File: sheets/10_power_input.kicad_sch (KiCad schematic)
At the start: 36 parts, among them J1 MSTB 2,5/5-GF-5,08, J2 MSTB 2,5/2-GF-5,08, Q101 STD18NF25, Q102 IPD30N10S3L-34, U101 LM74930QRGERQ1

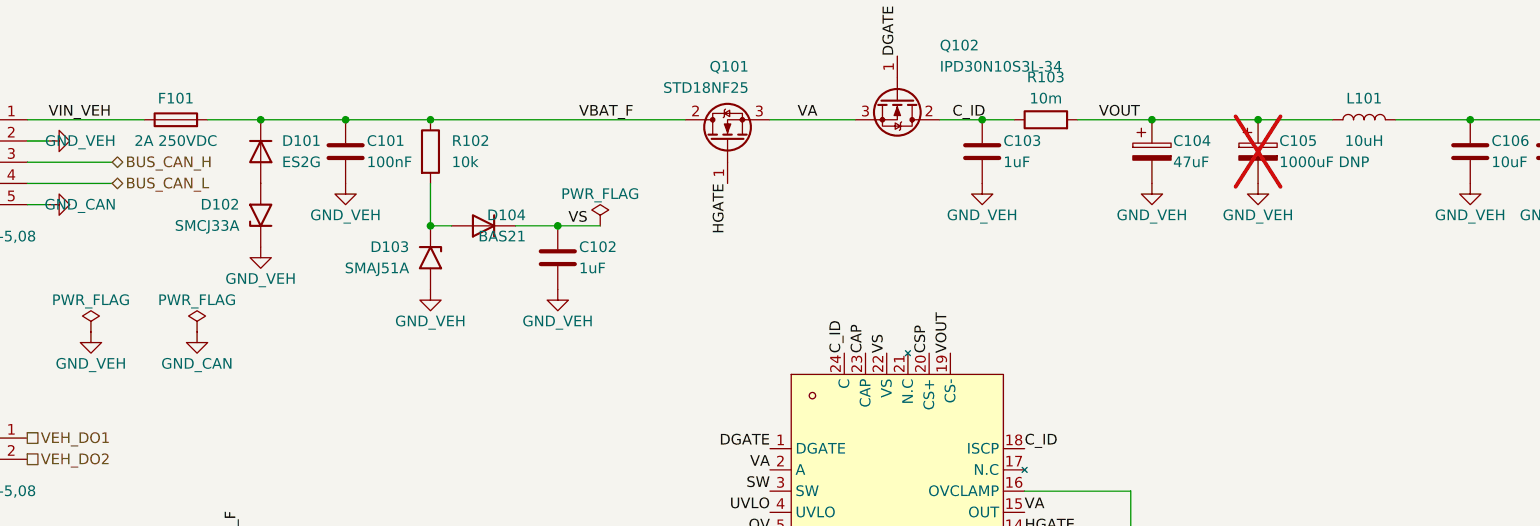
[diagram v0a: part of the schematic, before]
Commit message: [Claude Code] 60_can, 70_output, 10_power_input: criterio prototipo = producción, campo DNP
- 60_can: ADM3055E según datasheet Rev. D (tabla 10): FB602 separa GNDISO
  de GND2, VISOOUT con 0.22 uF + 10 uF, RS a GND2 por R605 (0 ohm), AUXIN a
  GND1, pull-up de STBY, ESD2CAN24-Q1 DNP; referencias 6xx y campos completos.
- 70_output: DMN10H220LQ (100 V, SOT-23), SMAJ58A, buffer 74AHCT1G126
  (3.3 -> 5 V), zener de gate; latch y diagnóstico como huellas DNP.
- 10_power_input: J1/J2 MSTB 2,5 de 5.08 mm GF (J2 = 1776508), F101
  SF-2410FPA200W-2, C105 hold-up DNP; se quita un PWR_FLAG suelto en GND_CAN.
- Campo DNP (vacío / PROTO / PROD / PROTO,PROD) en todos los símbolos.
- README y PENDIENTES: decisiones del usuario, máximos de la entrada,
  temas abiertos (buck de la opción B, R109, TVS de entrada grande).

Co-Authored-By: Claude Opus 5.5 <noreply@anthropic.com>
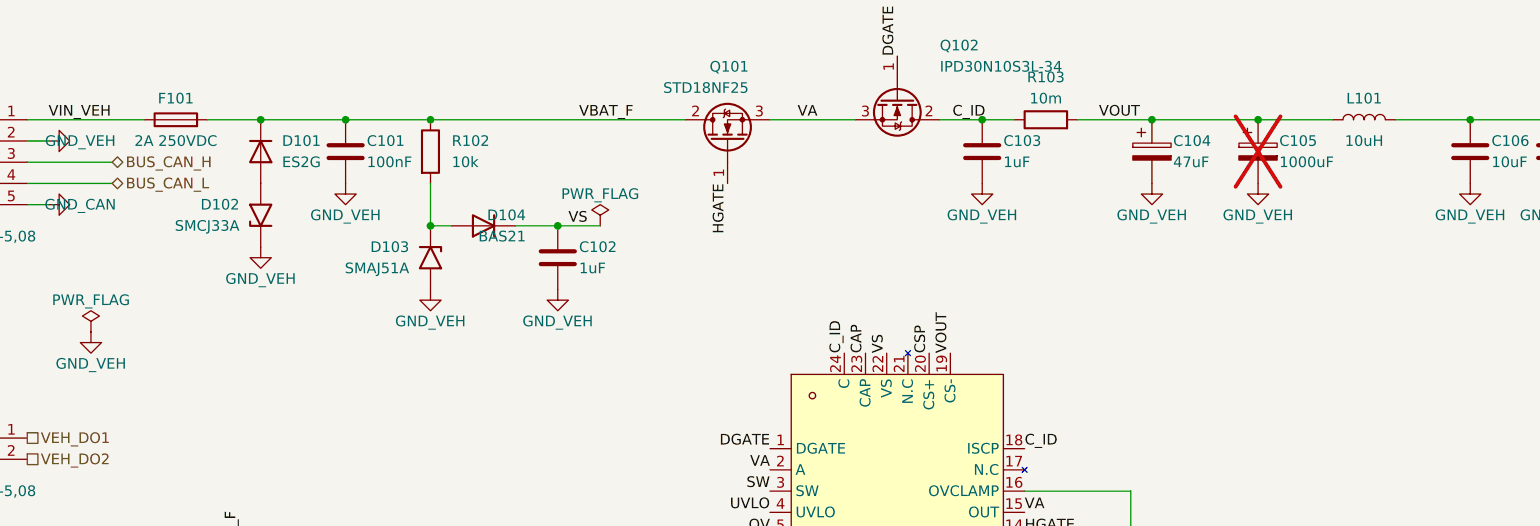
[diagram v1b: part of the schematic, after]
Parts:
- C105: value 1000uF DNP -> 1000uF; DNP (none) -> PROTO,PROD; Notes Hold-up de la lógica durante el corte por OV (~0.9-2.6 mF).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 -> Hold-up OPCIONAL (huella reservada, DNP): mantiene viva la 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
- F101: MPN PENDIENTE: Bourns SF-2410FPA-W, 2 A -> SF-2410FPA200W-2; Notes Fusible de falla grave (el limitador del LM74930 actúa ante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 -> Bourns SF-2410FPA200W-2: 2 A rapido, 250 VDC, AEC-Q200 (LCS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
- J1: footprint Connector_Phoenix_MC:PhoenixContact_MCV_1,5_5-GF-3.81_1x05_P3.81mm_Vertical_ThreadedFlange -> Connector_Phoenix_MSTB:PhoenixContact_MSTB_2,5_5-GF-5,08_1x05_P5.08mm_Horizontal_ThreadedFlange; Notes Enchufe: MSTB 2,5/5-STF-5,08 (1778014). Pines: 1 V+, 2 GND_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 -> Header MSTB 2,5/5-GF-5,08 (1776537) con brida roscada; ench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
- J2: footprint Connector_Phoenix_MC:PhoenixContact_MCV_1,5_2-GF-3.81_1x02_P3.81mm_Vertical_ThreadedFlange -> Connector_Phoenix_MSTB:PhoenixContact_MSTB_2,5_2-GF-5,08_1x02_P5.08mm_Horizontal_ThreadedFlange; MPN PENDIENTE (header MSTB 2,5/2-GF-5,08) -> 1776508; Notes Enchufe: MSTB 2,5/2-STF-5,08 (1777989). Pines: 1 DO1, 2 DO2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 -> Header MSTB 2,5/2-GF-5,08 (1776508) con brida roscada; ench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

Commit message: [Claude Code] 20_buck_5v: opción B (no aislada) con LMR38010; masas unificadas
- sheets/20_isolation -> sheets/20_buck_5v: se quitan PS201, ISO7763 y
  TPS7A1650; U201 LMR38010SQDDARQ1 (PROTO: LMR38010SDDAR, LCSC C5219310),
  5.02 V / 1 A a 400 kHz según TI SNVSC73B (L201 XAL6060-333, 3 x 22 uF,
  RT 64.9k, FB 100k/24.9k). Huella oficial HSOIC-8 con vías térmicas.
- Símbolo LMR38010 (easyeda2kicad) en lib/easyeda2kicad/INCLI-VA_easyeda,
  con tipos de pin ajustados; registrado en sym-lib-table.
- Todas las hojas: GND_ISO -> GND_VEH, +5V_ISO -> +5V_VEH.
- Raíz: EN/DIAG/FLT directos entre las hojas 40, 70 y 10; la hoja 20 sin pines.
- 10_power_input: R111 a +3V3_D, C109 = 100 nF (inrush con C105),
  C105 DNP solo en PROTO; se quita un PWR_FLAG suelto en GND_VEH.
- 70_output_ch: cambios de layout del usuario (hechos en KiCad).
- Textos de las hojas 30/40/50/80 y la raíz sin referencias al aislamiento.
- ERC: 0 en 10, 20, 30, 40, 50, 60 y 70; quedan los de 80 (hoja vacía).

Co-Authored-By: Claude Opus 5.5 <noreply@anthropic.com>
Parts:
- C105: DNP PROTO,PROD -> PROTO; Notes Hold-up OPCIONAL (huella reservada, DNP): mantiene viva la 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 -> Hold-up: DNP en PROTO, montado en PROD. Mantiene la logica 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
- C109: value 10nF -> 100nF; MPN GCM188R72A103KA37D -> GCM188R72A104KA64D; Notes C_dVdT: limita el inrush (100 V en 0603). -> C_dVdT (TI ec. 2): Iinrush = C_OUT x 55 uA / C_dVdT. Con C1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
- R111: Notes Pull-up de FLT (open drain). -> Pull-up de FLT (drenador abierto) a +3V3_D: PWR_FLT_N va di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
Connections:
- net +5V_VEH renamed +3V3_D
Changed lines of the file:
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@@
 			)
 		)
-		(property "Notes" "Hold-up OPCIONAL (huella reservada, DNP): mantiene viva la logica durante el corte por OV del LM74930 (load dump suprimido de 24 V, <= 350 ms) y los huecos de arranque en frio de 12 V (4.5-6 V, 15-40 ms). No hace falta para los pulsos ISO 7637 (rapidos). Sin C105 la placa se reinicia en esos eventos (estado funcional C). 1000-2200 uF / 50 V radial 16 mm."
+		(property "Notes" "Hold-up: DNP en PROTO, montado en PROD. Mantiene la logica en el corte por OV del LM74930 (load dump suprimido 24 V, <= 350 ms) y en el arranque en frio de 12 V (4.5-6 V, 15-40 ms). Energia 28->6 V: 0.37 J (~0.7 s a 0.5 W, ~0.25 s a 1.5 W con WiFi). Requiere C109 = 100 nF (inrush). PROD: electrolitico SMD automotriz AEC-Q200, >= 50 V, 105-125 C, version resistente a vibracion; MPN pendiente (ver PENDIENTES)."
 			(at 252.73 80.01 0)
 			(hide yes)
@@
 			)
 		)
-		(property "DNP" "PROTO,PROD"
+		(property "DNP" "PROTO"
 			(at 252.73 80.01 0)
 			(hide yes)
@@
 	(symbol
 		(lib_id "INCLI-VA:GND_VEH")
-		(at 113.03 101.6 0)
-		(unit 1)
-		(body_style 1)
-		(exclude_from_sim no)
-		(in_bom no)
-		(on_board yes)
-		(in_pos_files yes)
-		(dnp no)
-		(property "Reference" "#PWR124"
-			(at 113.03 108.08 0)
-			(hide yes)
-			(show_name no)
-			(do_not_autoplace no)
-			(effects
-				(font
-					(size 1.27 1.27)
-				)
-			)
-		)
-		(property "Value" "GND_VEH"
-			(at 113.03 105.41 0)
-			(show_name no)
-			(do_not_autoplace no)
-			(effects
-				(font
-					(size 1.27 1.27)
-				)
-			)
-		)
-		(property "Footprint" ""
-			(at 113.03 101.6 0)
-			(hide yes)
-			(show_name no)
-			(do_not_autoplace no)
-			(effects
-				(font
-					(size 1.27 1.27)
-				)
-			)
-		)
-		(property "Datasheet" ""
-			(at 113.03 101.6 0)
-			(hide yes)
-			(show_name no)
-			(do_not_autoplace no)
-			(effects
-				(font
-					(size 1.27 1.27)
-				)
-			)
-		)
-		(property "Description" ""
-			(at 113.03 101.6 0)
-			(show_name no)
-			(do_not_autoplace no)
-			(effects
-				(font
-					(size 1.27 1.27)
-				)
-			)
-		)
-		(pin "1"
-		)
-		(instances
-			(project "INCLI-VA"
-				(path "/7fd92c2b-4254-4d73-93ba-bfde861bede3/4b8ecaf5-3402-41a7-b174-dcc5b5a5cc30"
-					(reference "#PWR124")
-					(unit 1)
-				)
-			)
-		)
-	)
-	(symbol
-		(lib_id "INCLI-VA:GND_VEH")
 		(at 288.29 83.82 0)
 		(unit 1)
@@
 	)
 	(symbol
-		(lib_id "INCLI-VA:+5V_VEH")
+		(lib_id "INCLI-VA:+3V3_D")
 		(at 199.39 162.56 0)
 		(unit 1)
@@
 			)
 		)
-		(property "Value" "+5V_VEH"
+		(property "Value" "+3V3_D"
 			(at 199.39 158.75 0)
 			(show_name no)
@@
 			)
 		)
-		(property "Value" "10nF"
+		(property "Value" "100nF"
 			(at 191.77 175.26 0)
 			(show_name no)
@@
 			)
 		)
-		(property "Datasheet" "https://www.murata.com/en-us/products/productdetail?partno=GCM188R72A103KA37%23"
+		(property "Datasheet" "https://www.murata.com/en-global/products/productdetail?partno=GCM188R72A104KA64D"
 			(at 189.23 173.99 0)
 			(hide yes)
@@
 			)
 		)
-		(property "MPN" "GCM188R72A103KA37D"
+		(property "MPN" "GCM188R72A104KA64D"
 			(at 189.23 173.99 0)
 			(hide yes)
@@
 			)
 		)
-		(property "Notes" "C_dVdT: limita el inrush (100 V en 0603)."
+		(property "Notes" "C_dVdT (TI ec. 2): Iinrush = C_OUT x 55 uA / C_dVdT. Con C105 montado (~1.07 mF): 0.59 A < breaker 1 A (con 10 nF eran 5.9 A y disparaba). Sin C105: ~34 mA. Arranque ~60 ms. 100 V en 0603."
 			(at 189.23 173.99 0)
 			(hide yes)
@@
 			)
 		)
-		(property "Notes" "Pull-up de FLT (open drain)."
+		(property "Notes" "Pull-up de FLT (drenador abierto) a +3V3_D: PWR_FLT_N va directo a un GPIO del ESP32 (opcion B)."
 			(at 199.39 166.37 0)
 			(hide yes)
@@
 					(unit 1)
 				)
-			)
-		)
-	)
-	(symbol
-		(lib_id "power:PWR_FLAG")
-		(at 113.03 101.6 0)
-		(unit 1)
-		(body_style 1)
-		(exclude_from_sim no)
-		(in_bom no)
-		(on_board yes)
-		(in_pos_files yes)
-		(dnp no)
-		(property "Reference" "#FLG123"
-			(at 113.03 95.12 0)
-			(hide yes)
-			(show_name no)
-			(do_not_autoplace no)
-			(effects
-				(font
-					(size 1.27 1.27)
-				)
-			)
-		)
-		(property "Value" "PWR_FLAG"
-			(at 113.03 97.79 0)
-			(show_name no)
-			(do_not_autoplace no)
-			(effects
-				(font
-					(size 1.27 1.27)
-				)
-			)
-		)
-		(property "Footprint" ""
-			(at 113.03 101.6 0)
-			(hide yes)
-			(show_name no)
-			(do_not_autoplace no)
-			(effects
-				(font
-					(size 1.27 1.27)
-				)
-			)
-		)
-		(property "Datasheet" ""
-			(at 113.03 101.6 0)
-			(hide yes)
-			(show_name no)
-			(do_not_autoplace no)
-			(effects
-				(font
-					(size 1.27 1.27)
-				)
-			)
-		)
-		(property "Description" ""
-			(at 113.03 101.6 0)
-			(show_name no)
-			(do_not_autoplace no)
-			(effects
-				(font
-					(size 1.27 1.27)
-				)
-			)
-		)
-		(pin "1"
-		)
-		(instances
-			(project "INCLI-VA"
-				(path "/7fd92c2b-4254-4d73-93ba-bfde861bede3/4b8ecaf5-3402-41a7-b174-dcc5b5a5cc30"
-					(reference "#FLG123")
-					(unit 1)
-				)

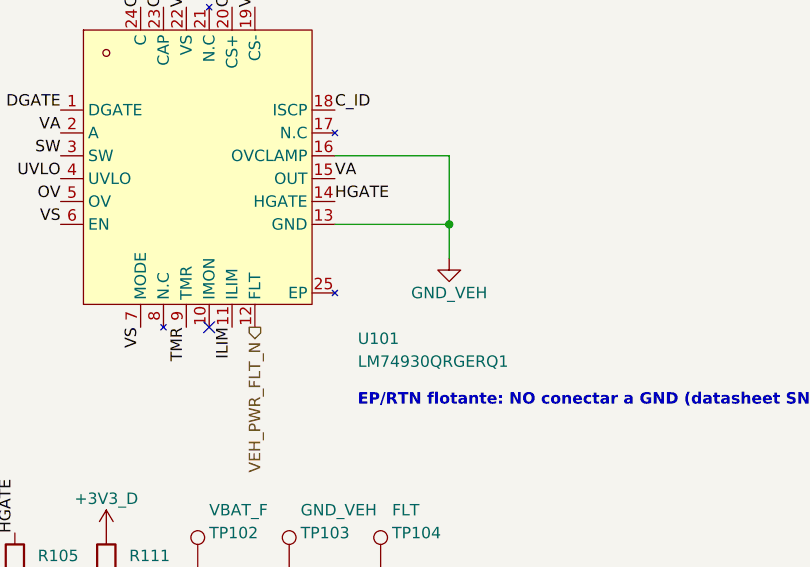
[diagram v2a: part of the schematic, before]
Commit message: [Claude Code] DRU para JLCPCB, red U101_RTN y limpieza de librerías
- INCLI-VA.kicad_dru: capacidades de JLCPCB (2 capas, 1 oz, 1.6 mm) con
  margen; separación HV en la entrada (1.25 mm, IPC-2221B B2), DO y
  +VPROT (0.6 mm); barrera del ADM3055E (2.5 mm + sin relleno bajo U601);
  anchos IPC-2152 (entrada 1.0 mm, DO y 5 V 0.5 mm); reglas para el pad 25
  de U101 (aislado y nunca GND, probado en una copia).
- U101 pin 25 (EP): no_connect -> passive en la librería y la caché;
  etiqueta U101_RTN en 10_power_input. En el PCB, las 7 redes
  unconnected-(U101-EP-Pad25)_N quedan como /10_power_input/U101_RTN
  (sin Update PCB from Schematic).
- Se borran las huellas y modelos 3D de URB2405 y HVSSOP-8, fp-lib-table.bak
  y lib/Connector_Phoenix_MSTB.pretty.bak/.
- PENDIENTES: reglas y fuentes, estado del DRC, propuesta de la hoja 80.

Co-Authored-By: Claude Opus 5.5 <noreply@anthropic.com>
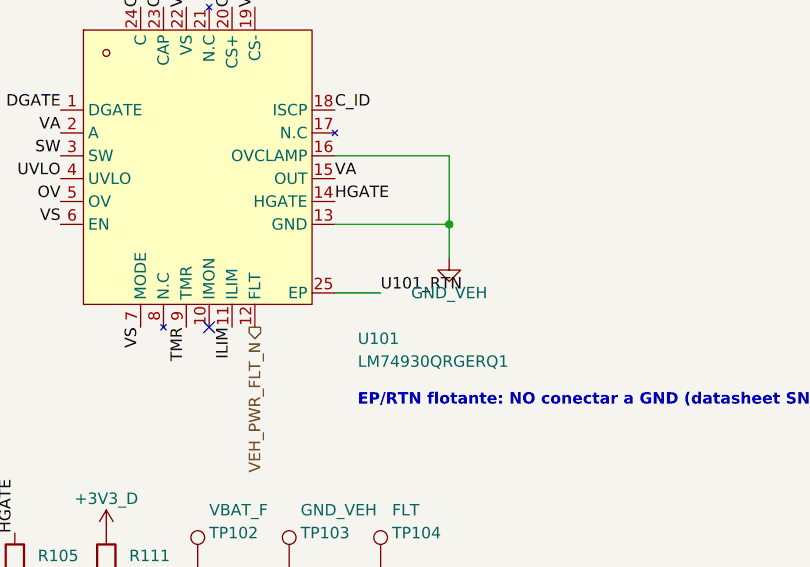
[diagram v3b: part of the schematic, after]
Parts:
- U101: Notes VQFN-24 aceptado para el demo. Pad expuesto = RTN: dejar FLOTANTE (TI), no conectar a GND. Huella INCLI-VA (corregida desde RGE0024T): paso exacto, pasta 4x0.94 mm, 5 vías a isla aislada en B.Cu (RTN), courtyard +-2.7 mm. LCSC C22428070. -> VQFN-24 aceptado para el demo. Pad expuesto = RTN: dejar FLOTANTE (TI), no conectar a GND. Huella INCLI-VA (corregida desde RGE0024T): paso exacto, pasta 4x0.94 mm, 5 vías a isla aislada en B.Cu (RTN), courtyard +-2.7 mm. LCSC C22428070. Pin 25 (EP/RTN) -> red U101_RTN: un solo nombre para todos los pads 25 de la huella (EP + vias + isla en B.Cu). NUNCA a GND (TI SNOSDF6, tabla 5-1 y 8.3). Regla en INCLI-VA.kicad_dru.
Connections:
- net U101_RTN: now reaches U101.25 (EP)
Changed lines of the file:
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@@
 			)
 		)
-		(property "Notes" "VQFN-24 aceptado para el demo. Pad expuesto = RTN: dejar FLOTANTE (TI), no conectar a GND. Huella INCLI-VA (corregida desde RGE0024T): paso exacto, pasta 4x0.94 mm, 5 vías a isla aislada en B.Cu (RTN), courtyard +-2.7 mm. LCSC C22428070."
+		(property "Notes" "VQFN-24 aceptado para el demo. Pad expuesto = RTN: dejar FLOTANTE (TI), no conectar a GND. Huella INCLI-VA (corregida desde RGE0024T): paso exacto, pasta 4x0.94 mm, 5 vías a isla aislada en B.Cu (RTN), courtyard +-2.7 mm. LCSC C22428070. Pin 25 (EP/RTN) -> red U101_RTN: un solo nombre para todos los pads 25 de la huella (EP + vias + isla en B.Cu). NUNCA a GND (TI SNOSDF6, tabla 5-1 y 8.3). Regla en INCLI-VA.kicad_dru."
 			(at 209.55 121.92 0)
 			(hide yes)
@@
 		)
 	)
+	(wire
+		(pts
+			(xy 224.79 135.89) (xy 229.87 135.89)
+		)
+		(stroke
+			(width 0)
+			(type default)
+		)
+	)
+	(label "U101_RTN"
+		(at 229.87 135.89 0)
+		(effects
+			(font
+				(size 1.27 1.27)
+			)
+			(justify left bottom)
+		)
+	)

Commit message: [Claude Code] 80_supervision: TPS3828-33-Q1, LED y VAR_ID; J1/J2 verticales; contorno con muesca
- 80_supervision: U801 TPS3828-33QDBVRQ1 (supervisor de +3V3_D + watchdog,
  WDI <- IO17), R802 0 ohm, R801 DNP; LED verde/rojo DNP en PROD (caja
  opaca); VAR_ID0/1 (CAN/OUT) y VAR_ID2 (IO8, CABIN, DNP).
- WD_EN eliminado (IO18 libre); VAR_ID2 ocupa su pin en las hojas 40/80 y la raíz.
- 10_power_input: J1/J2 MSTBV 2,5 GF 5.08 verticales (1777109 / 1777073).
- lib: se borran los símbolos URB2405 y TPS7A1650; U101: vías del EP a Ø 0.45 mm.
- PCB: contorno único con muesca de 8 x 35 mm para la antena (antes, dos
  rectángulos superpuestos); serigrafía de U401 recortada en la muesca.
- ERC: 0 errores, 1 aviso intencional (U101_RTN).

Co-Authored-By: Claude Opus 5.5 <noreply@anthropic.com>
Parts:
- J1: value MSTB 2,5/5-GF-5,08 -> MSTBV 2,5/5-GF-5,08; footprint Connector_Phoenix_MSTB:PhoenixContact_MSTB_2,5_5-GF-5,08_1x05_P5.08mm_Horizontal_ThreadedFlange -> Connector_Phoenix_MSTB:PhoenixContact_MSTBV_2,5_5-GF-5,08_1x05_P5.08mm_Vertical_ThreadedFlange; MPN 1776537 -> 1777109; Notes Header MSTB 2,5/5-GF-5,08 (1776537) con brida roscada; ench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 -> Header vertical MSTBV 2,5/5-GF-5,08 (1777109) con brida ros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
- J2: value MSTB 2,5/2-GF-5,08 -> MSTBV 2,5/2-GF-5,08; footprint Connector_Phoenix_MSTB:PhoenixContact_MSTB_2,5_2-GF-5,08_1x02_P5.08mm_Horizontal_ThreadedFlange -> Connector_Phoenix_MSTB:PhoenixContact_MSTBV_2,5_2-GF-5,08_1x02_P5.08mm_Vertical_ThreadedFlange; MPN 1776508 -> 1777073; Notes Header MSTB 2,5/2-GF-5,08 (1776508) con brida roscada; ench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 -> Header vertical MSTBV 2,5/2-GF-5,08 (1777073, VERIFICAR en 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
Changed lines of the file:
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@@
 			)
 		)
-		(property "Value" "MSTB 2,5/5-GF-5,08"
+		(property "Value" "MSTBV 2,5/5-GF-5,08"
 			(at 97.79 90.17 0)
 			(show_name no)
@@
 			)
 		)
-		(property "Footprint" "Connector_Phoenix_MSTB:PhoenixContact_MSTB_2,5_5-GF-5,08_1x05_P5.08mm_Horizontal_ThreadedFlange"
+		(property "Footprint" "Connector_Phoenix_MSTB:PhoenixContact_MSTBV_2,5_5-GF-5,08_1x05_P5.08mm_Vertical_ThreadedFlange"
 			(at 100.33 81.28 0)
 			(hide yes)
@@
 			)
 		)
-		(property "Datasheet" "https://www.phoenixcontact.com/en-us/products/1776537"
+		(property "Datasheet" "https://www.phoenixcontact.com/en-us/products/1777109"
 			(at 100.33 81.28 0)
 			(hide yes)
@@
 			)
 		)
-		(property "MPN" "1776537"
+		(property "MPN" "1777109"
 			(at 100.33 81.28 0)
 			(hide yes)
@@
 			)
 		)
-		(property "Notes" "Header MSTB 2,5/5-GF-5,08 (1776537) con brida roscada; enchufe MSTB 2,5/5-STF-5,08 (1778014). Pines: 1 V+, 2 GND_VEH, 3 CAN_H, 4 CAN_L, 5 CAN_GND. 320 V / 12 A."
+		(property "Notes" "Header vertical MSTBV 2,5/5-GF-5,08 (1777109) con brida roscada; enchufe MSTB 2,5/5-STF-5,08 (1778014). Pines: 1 V+, 2 GND_VEH, 3 CAN_H, 4 CAN_L, 5 CAN_GND. 320 V / 12 A. Cableado interno hasta el conector circular de 8 hilos de la caja."
 			(at 100.33 81.28 0)
 			(hide yes)
@@
 			)
 		)
-		(property "Value" "MSTB 2,5/2-GF-5,08"
+		(property "Value" "MSTBV 2,5/2-GF-5,08"
 			(at 97.79 120.65 0)
 			(show_name no)
@@
 			)
 		)
-		(property "Footprint" "Connector_Phoenix_MSTB:PhoenixContact_MSTB_2,5_2-GF-5,08_1x02_P5.08mm_Horizontal_ThreadedFlange"
+		(property "Footprint" "Connector_Phoenix_MSTB:PhoenixContact_MSTBV_2,5_2-GF-5,08_1x02_P5.08mm_Vertical_ThreadedFlange"
 			(at 100.33 114.3 0)
 			(hide yes)
@@
 			)
 		)
-		(property "Datasheet" "https://www.phoenixcontact.com/en-us/products/1776508"
+		(property "Datasheet" "https://www.phoenixcontact.com/en-us/products/1777073"
 			(at 100.33 114.3 0)
 			(hide yes)
@@
 			)
 		)
-		(property "MPN" "1776508"
+		(property "MPN" "1777073"
 			(at 100.33 114.3 0)
 			(hide yes)
@@
 			)
 		)
-		(property "Notes" "Header MSTB 2,5/2-GF-5,08 (1776508) con brida roscada; enchufe MSTB 2,5/2-STF-5,08 (1777989). Pines: 1 DO1, 2 DO2 (low-side; drenador hasta 58 V + pico inductivo recortado < 100 V). Colocar la proteccion de 70_output junto a J2."
+		(property "Notes" "Header vertical MSTBV 2,5/2-GF-5,08 (1777073, VERIFICAR en phoenixcontact.com) con brida roscada; enchufe MSTB 2,5/2-STF-5,08 (1777989). Pines: 1 DO1, 2 DO2 (low-side; drenador hasta 58 V + pico inductivo recortado < 100 V). Colocar la proteccion de 70_output junto a J2."
 			(at 100.33 114.3 0)
 			(hide yes)
